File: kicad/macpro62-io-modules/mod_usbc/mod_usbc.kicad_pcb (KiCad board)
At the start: 2 copper layers, 38.8 x 8.8 mm, 5 parts, among them J1 MOD-C - HOAUC HYCW417-USBC24-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, J2 DF40C-50DP-0.4V(51) C424645 -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, U1 24C02 WLCSP-4 ID EEPROM @0x50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

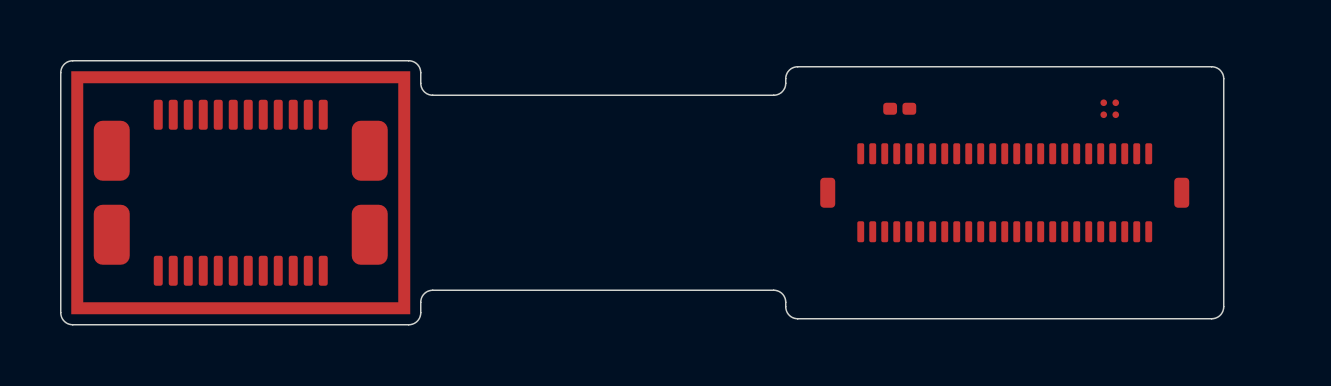
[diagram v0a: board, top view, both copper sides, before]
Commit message: I/O plate: centre + corner M1.6 frame screws, screwpt variant, plate fixes, module routing, ESD
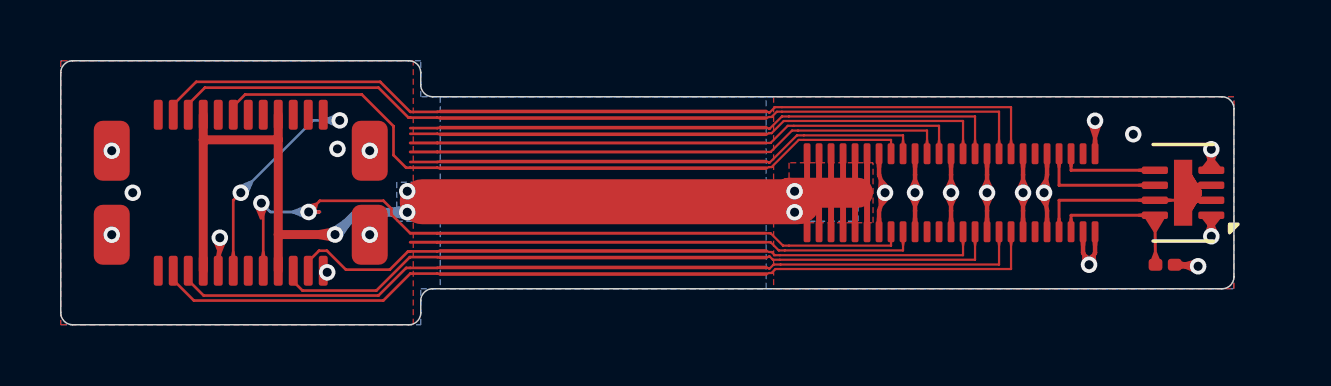
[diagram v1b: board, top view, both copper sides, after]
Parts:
- removed G1: sleeve GND ring (SUS304 0.2 sleeve, bonded to the shell), MP62_MOD:MP62_MOD_Sleeve_GND_Ring_USBC
- C1: value 100nF 0201 (3V3_MOD) -> 100nF 0201 X5R 10V (3V3_MOD)
- J2: value DF40C-50DP-0.4V(51) C424645 -> main-board JMn DF40C-50DS (PMI-50 pinout) -> DF40C-50DP-0.4V(51) C424645 -> JMn DF40C-50DS (PMI-50 v2)
- U1: value 24C02 WLCSP-4 ID EEPROM @0x50 (MOD ID / type / rev / serial) -> BL24C02F-NTRC (C2828222) 24C02 ID EEPROM @0x50; footprint MP62_MOD:MP62_WLCSP-4_0.8x0.8_P0.4_EEPROM -> MP62_MOD:DFN-8-1EP_2x3mm_P0.5mm_EP0.61x2.2mm
- moved C1 10.3 mm to (130.8, 102.4)
- moved U1 3.72 mm to (131.4, 100.0), turned to 180 degrees
- moved J2 1.79 mm to (123.7, 100.0)
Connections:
- C1 pad 1: (no net) -> 3V3_MOD
- C1 pad 2: (no net) -> GND
- J1 pad A1: (no net) -> GND
- J1 pad A10: (no net) -> SSRX2_N
- J1 pad A11: (no net) -> SSRX2_P
- J1 pad A12: (no net) -> GND
- J1 pad A2: (no net) -> SSTX1_P
- J1 pad A3: (no net) -> SSTX1_N
- J1 pad A4: (no net) -> VBUS
- J1 pad A5: (no net) -> CC1
- J1 pad A6: (no net) -> D_P
- J1 pad A7: (no net) -> D_N
- J1 pad A8: (no net) -> SBU1
- J1 pad A9: (no net) -> VBUS
- J1 pad B1: (no net) -> GND
- J1 pad B10: (no net) -> SSRX1_N
- J1 pad B11: (no net) -> SSRX1_P
- J1 pad B12: (no net) -> GND
- J1 pad B2: (no net) -> SSTX2_P
- J1 pad B3: (no net) -> SSTX2_N
- J1 pad B4: (no net) -> VBUS
- J1 pad B5: (no net) -> CC2
- J1 pad B6: (no net) -> D_P
- J1 pad B7: (no net) -> D_N
- J1 pad B8: (no net) -> SBU2
- J1 pad B9: (no net) -> VBUS
- J1 pad S: (no net) -> GND
- J2 pad 1: (no net) -> VBUS
- J2 pad 10: (no net) -> VBUS
- J2 pad 11: (no net) -> VBUS
- J2 pad 12: (no net) -> VBUS
- J2 pad 13: (no net) -> GND
- J2 pad 14: (no net) -> GND
- J2 pad 15: (no net) -> D_P
- J2 pad 16: (no net) -> CC2
- J2 pad 17: (no net) -> D_N
- J2 pad 18: (no net) -> SBU2
- J2 pad 19: (no net) -> GND
- J2 pad 2: (no net) -> VBUS
- J2 pad 20: (no net) -> GND
- J2 pad 21: (no net) -> CC1
- J2 pad 23: (no net) -> SBU1
- J2 pad 25: (no net) -> GND
- J2 pad 26: (no net) -> GND
- J2 pad 27: (no net) -> SSRX2_P
- J2 pad 28: (no net) -> SSTX2_P
- J2 pad 29: (no net) -> SSRX2_N
- J2 pad 3: (no net) -> VBUS
- J2 pad 30: (no net) -> SSTX2_N
- J2 pad 31: (no net) -> GND
- J2 pad 32: (no net) -> GND
- J2 pad 33: (no net) -> SSTX1_N
- J2 pad 34: (no net) -> SSRX1_N
- J2 pad 35: (no net) -> SSTX1_P
- J2 pad 36: (no net) -> SSRX1_P
- J2 pad 37: (no net) -> GND
- J2 pad 38: (no net) -> GND
- J2 pad 4: (no net) -> VBUS
- J2 pad 41: (no net) -> GND
- J2 pad 42: (no net) -> GND
- J2 pad 43: (no net) -> ID_SCL
- J2 pad 44: (no net) -> GND
- J2 pad 45: (no net) -> ID_SDA
- J2 pad 46: (no net) -> 3V3_MOD
- J2 pad 48: (no net) -> GND
- J2 pad 49: (no net) -> GND
- J2 pad 5: (no net) -> VBUS
- J2 pad 50: (no net) -> GND
- J2 pad 6: (no net) -> VBUS
- J2 pad 7: (no net) -> VBUS
- J2 pad 8: (no net) -> VBUS
- J2 pad 9: (no net) -> VBUS
- U1 pad 1: (no net) -> GND
- U1 pad 2: (no net) -> GND
- U1 pad 3: (no net) -> GND
- U1 pad 4: (no net) -> GND
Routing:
- net VBUS: track 0.00 -> 48.9 mm, vias 0 -> 5
- net SSTX1_P: track 0.00 -> 30.6 mm
- net SSRX1_P: track 0.00 -> 30.2 mm
- net SSTX1_N: track 0.00 -> 29.5 mm
- net SSRX1_N: track 0.00 -> 29.1 mm
- net GND: track 0.00 -> 28.3 mm, vias 0 -> 19
- net CC2: track 0.00 -> 26.4 mm, vias 0 -> 2
- net D_P: track 0.00 -> 24.8 mm
- net SSTX2_N: track 0.00 -> 24.7 mm
- net D_N: track 0.00 -> 24.6 mm, vias 0 -> 2
- net SSTX2_P: track 0.00 -> 23.6 mm
- net SSRX2_N: track 0.00 -> 20.2 mm
- net SSRX2_P: track 0.00 -> 19.7 mm
- net SBU1: track 0.00 -> 18.8 mm
- net CC1: track 0.00 -> 18.3 mm
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- added copper zone on B.Cu, net GND
- added copper zone on F.Cu, net GND
- added copper zone on B.Cu, net VBUS
- added copper zone on F.Cu, net VBUS
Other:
- board size 38.8 x 8.8 mm -> 39.1 x 8.8 mm
- board text added: "C-fold 180 deg, R 3.26-3.30 = 17-17 x t (bend zone: no vias / parts, hatched L2)"
- board text added: "FR4 0.6 stiffener (B) under the header paddle"
- board text added: "FR4 1.0 stiffener (B, PSA) under the port"
- board text added: "cradle ledges (stiffener bottom bears here, 1.0 wide)"
- board text removed: "C-fold 180 deg, R 3.24 (bend zone: no vias, no parts, staggered traces)"
- board text removed: "FR4 1.0 stiffener (B) under the header paddle"
- board text removed: "FR4 1.0 stiffener (B, flush, PSA) under the port"
- board text removed: "Fits slots C1, C2, C3, C4, C5, C6. Electrical length port pads -> header ~28 mm."
- board text removed: "MOD-C, unfolded. Port at (0,0); u -> outboard edge. Stiffener 12.0 x 8.8; tail 6.5 wide; flap 1.5; fold R 3.24; paddle 14.6 x 8.4."
- board text removed: "PMI-50 (J2 odd/even): 13/14 GND/GND; 15/16 GND/GND; 17/18 HS0_P/HS2_P; 19/20 HS0_N/HS2_N; 21/22 GND/GND; 23/24 HS1_P/HS3_P; 25/26 HS1_N/HS3_N; 27/28 GND/GND; 29/30 USB2_DP/SBU1; 31/32 USB2_DN/SBU2; 33/34 GND/GND; 35/36 CC1/HPD; 37/38 CC2/UTIL; 39/40 GND/GND; 41/42 ID_SCL/ID_SDA; 43/44 3V3_MOD/PRSNT#; 45/46 LED#/GND; 47/48 GND/GND; 49/50 GND/GND"
- board text removed: "Plug loads: push -> connector body -> FPC -> FR4 stiffener -> cradle ledges; pull/side -> bonded SUS sleeve -> collar -> clamp plate -> screws. Not through solder or flex."
- board text removed: "cradle ledges (stiffener bottom bears here; no parts / THT tips in the bands)"
- board text removed: "optional silver EMI film (F), >= 0.8 from stiffeners, GND openings D1.0 at both ends"

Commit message: USB-C flex module routed (HYCW417, 0 DRC, matched pairs), 3-mil min on flexes, two flex panels, CH334F + ASM1182e QFN-48 footprints
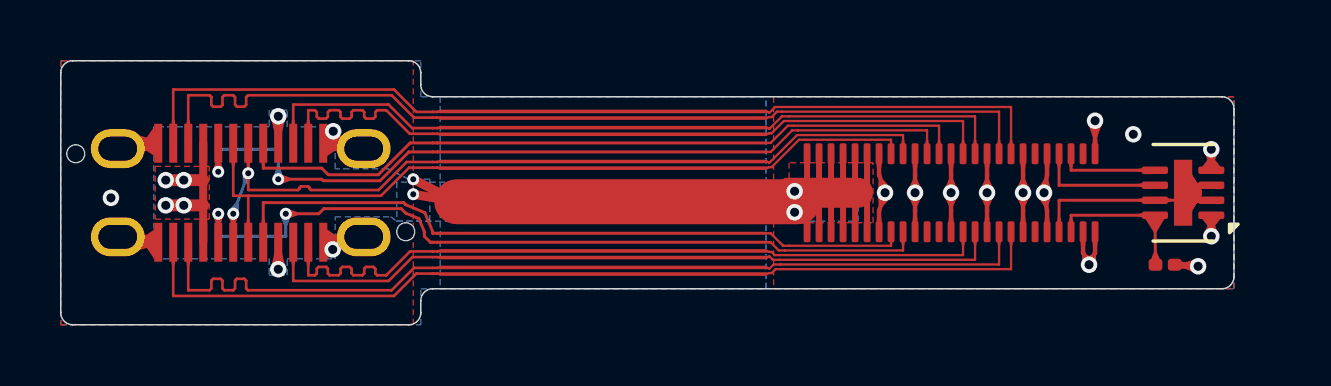
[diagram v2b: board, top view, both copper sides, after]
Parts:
- J1: value MOD-C - HOAUC HYCW417-USBC24-180B (C5342202) all-SMD -> MOD-C - HOAUC HYCW417-USBC24-180B (C5342202) SMD + 4 THT shell legs 1.8; footprint MP62_MOD:MP62_MOD_USB_C_24P_Vertical_SMD_PLACEHOLDER -> MP62_MOD:HOAUC_HYCW417-USBC24-180B
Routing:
- net CC1: track 18.3 -> 27.8 mm, vias 0 -> 2
- net VBUS: track 48.9 -> 40.3 mm, vias 5 -> 10
- net SBU2: track 18.3 -> 26.7 mm, vias 1 -> 2
- net SBU1: track 18.8 -> 25.1 mm
- net SSRX2_P: track 19.7 -> 25.8 mm
- net SSRX2_N: track 20.2 -> 25.8 mm
- net GND: track 28.3 -> 31.6 mm, vias 19 -> 15
- net CC2: track 26.4 -> 23.4 mm, vias 2 -> 0
- net D_N: track 24.6 -> 27.3 mm
- net SSRX1_N: track 29.1 -> 31.3 mm
- net SSTX1_N: track 29.5 -> 31.7 mm
- net SSTX2_P: track 23.6 -> 25.3 mm
- net D_P: track 24.8 -> 26.5 mm
- net SSRX1_P: track 30.2 -> 31.3 mm
- net SSTX1_P: track 30.6 -> 31.7 mm
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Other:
- board text added: "stiffener openings: 4 x 2.0 x 1.5 (shell legs), 2 x 0.9 (pegs)"

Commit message: Plate test-print fixes (corners +1mm Y, C2 post -1mm, C1 removed); USB-A/HDMI hand fan-out 0 skew; real DF40 + HDMI footprints
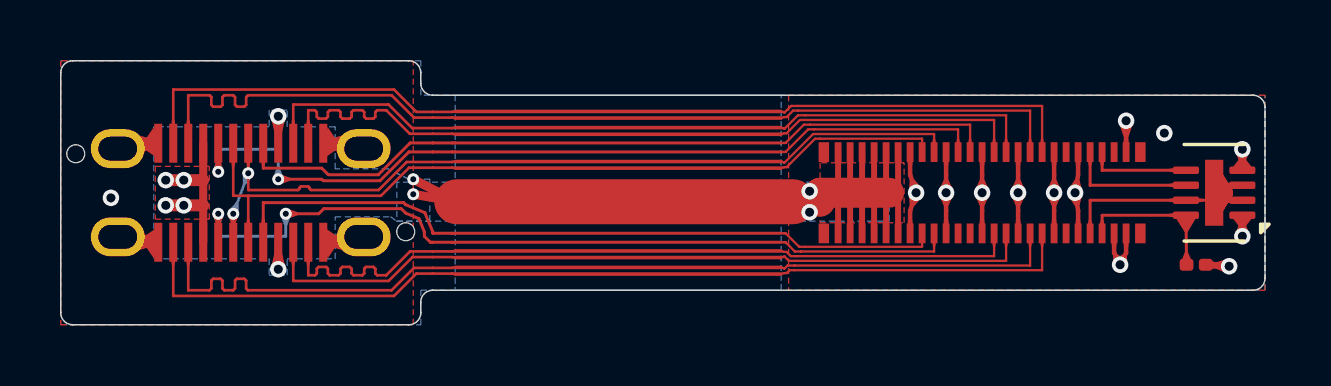
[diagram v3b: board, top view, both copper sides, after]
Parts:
- J2: footprint MP62_MOD:MP62_Hirose_DF40C-50DP-0.4V_PLACEHOLDER -> MP62_MOD:MP62_Hirose_DF40C-50DP-0.4V
- moved J2 1.04 mm to (124.7, 100.0)
- moved C1 1.03 mm to (131.8, 102.4)
- moved U1 1.03 mm to (132.4, 100.0)
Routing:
- net D_P: track 26.5 -> 27.5 mm
- net SSTX1_P: track 31.7 -> 32.7 mm
- net CC2: track 23.4 -> 24.5 mm
- net SBU1: track 25.1 -> 26.1 mm
- net CC1: track 27.8 -> 28.9 mm
- net SSTX2_P: track 25.3 -> 26.4 mm
- net SBU2: track 26.7 -> 27.7 mm
- net D_N: track 27.3 -> 28.3 mm
- net SSRX2_N: track 25.8 -> 26.8 mm
- net SSTX2_N: track 25.3 -> 26.4 mm
- net SSTX1_N: track 31.7 -> 32.7 mm
- net SSRX2_P: track 25.8 -> 26.8 mm
- net SSRX1_P: track 31.3 -> 32.3 mm
- net SSRX1_N: track 31.3 -> 32.3 mm
- net GND: track 31.6 -> 32.1 mm, vias 15 -> 13
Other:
- board size 39.1 x 8.8 mm -> 40.1 x 8.8 mm
